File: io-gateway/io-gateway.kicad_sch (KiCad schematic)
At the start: 8 parts, among them J1 1752201, J2 1752201, J3 1752201, J4 Screw_Terminal_01x09, J5 Screw_Terminal_01x09, J6 Screw_Terminal_01x09

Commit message: upd
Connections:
- net GND_DIM5 renamed Dimmer5/GND_DIM
- net VIN_DIM5 renamed Dimmer5/VIN_DIM
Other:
- added sheet Dimmer5 (dimmer1.kicad_sch)
- moved on the sheet: J3

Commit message: upd
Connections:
- net GND: now also J4.3 (Pin_3), J4.6 (Pin_6), J4.9 (Pin_9), J5.3 (Pin_3), J5.6 (Pin_6), J5.9 (Pin_9), J6.3 (Pin_3), J6.6 (Pin_6), J6.9 (Pin_9)
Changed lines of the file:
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@@
+		)
+	)
+	(label "GND_CTRL"
+		(at 220.98 31.75 0)
+		(effects
+			(font
+				(size 1.27 1.27)
+			)
+			(justify left bottom)
 		)
 	)
 	(label "VDC_CTRL"
 		(at 40.64 27.94 0)
+		(effects
+			(font
+				(size 1.27 1.27)
+			)
+			(justify left bottom)
+		)
+	)
+	(label "GND_CTRL"
+		(at 220.98 96.52 0)
 		(effects
 			(font
@@
 		)
 	)
+	(label "GND_CTRL"
+		(at 220.98 39.37 0)
+		(effects
+			(font
+				(size 1.27 1.27)
+			)
+			(justify left bottom)
+		)
+	)
+	(label "GND_CTRL"
+		(at 220.98 129.54 0)
+		(effects
+			(font
+				(size 1.27 1.27)
+			)
+			(justify left bottom)
+		)
+	)
 	(label "ANALOG_IN_1"
 		(at 40.64 38.1 0)
@@
 		)
 	)
+	(label "GND_CTRL"
+		(at 220.98 81.28 0)
+		(effects
+			(font
+				(size 1.27 1.27)
+			)
+			(justify left bottom)
+		)
+	)
+	(label "GND_CTRL"
+		(at 220.98 88.9 0)
+		(effects
+			(font
+				(size 1.27 1.27)
+			)
+			(justify left bottom)
+		)
+	)
+	(label "GND_CTRL"
+		(at 220.98 137.16 0)
+		(effects
+			(font
+				(size 1.27 1.27)
+			)
+			(justify left bottom)
+		)
+	)
+	(label "GND_CTRL"
+		(at 220.98 121.92 0)
+		(effects
+			(font
+				(size 1.27 1.27)
+			)
+			(justify left bottom)
+		)
+	)
 	(label "RS485_B"
 		(at 40.64 35.56 0)
 		(effects
 			(font
+				(size 1.27 1.27)
+			)
+			(justify left bottom)
+		)
+	)
+	(label "GND_CTRL"
+		(at 220.98 46.99 0)
+		(effects
+			(font

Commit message: upd
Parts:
- removed J4, J5, J6: Screw_Terminal_01x09, TerminalBlock_TE-Connectivity:TerminalBlock_TE_282836-9_1x09_P5mm_Horizontal, symbol Connector:Screw_Terminal_01x09
- added J10, J11, J12, J13, J4, J5, J7, J8, J9: Screw_Terminal_01x02, TerminalBlock:TerminalBlock_MaiXu_MX126-5.0-02P_1x02_P5.00mm, symbol Connector:Screw_Terminal_01x02
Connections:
- net Relay4/VAC_IN: now also J4.2 (Pin_2)
- net Relay4/VAC_OUT: now also J4.1 (Pin_1)
- net Relay5/VAC_IN: now also J10.2 (Pin_2)
- net Relay5/VAC_OUT: now also J10.1 (Pin_1)
- net Relay6/VAC_IN: now also J11.2 (Pin_2)
- net Relay6/VAC_OUT: now also J11.1 (Pin_1)
- net Relay7/VAC_IN: now also J5.2 (Pin_2)
- net Relay7/VAC_OUT: now also J5.1 (Pin_1)
- net Relay8/VAC_IN: now also J12.2 (Pin_2)
- net Relay8/VAC_OUT: now also J12.1 (Pin_1)
- net Relay9/VAC_IN: now also J13.2 (Pin_2)
- net Relay9/VAC_OUT: now also J13.1 (Pin_1)
- net VAC_IN_1: now also J7.2 (Pin_2)
- net VAC_IN_2: now also J8.2 (Pin_2)
- net VAC_IN_3: now also J9.2 (Pin_2)
- net VAC_OUT_1.1: now also J7.1 (Pin_1)
- net VAC_OUT_2.1: now also J8.1 (Pin_1)
- net VAC_OUT_3.1: now also J9.1 (Pin_1)

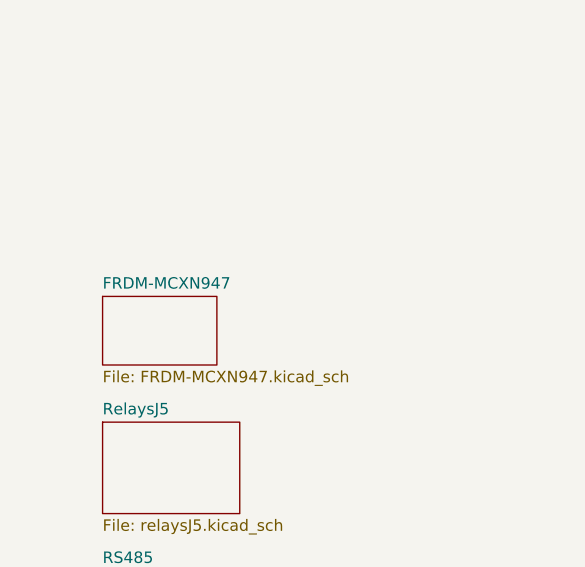
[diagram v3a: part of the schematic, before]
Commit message: connect Relays in Schematics
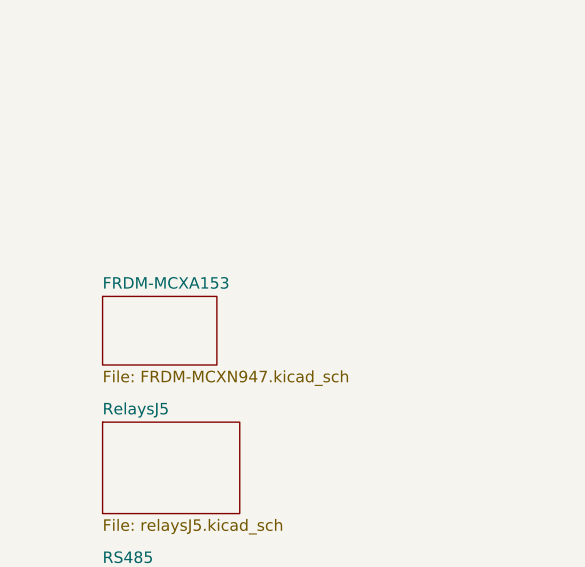
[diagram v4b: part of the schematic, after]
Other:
- sheet FRDM-MCXN947 renamed FRDM-MCXA153
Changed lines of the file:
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@@
 			(color 0 0 0 0.0000)
 		)
-		(property "Sheetname" "FRDM-MCXN947"
+		(property "Sheetname" "FRDM-MCXA153"
 			(at 30.48 218.9984 0)
 			(effects

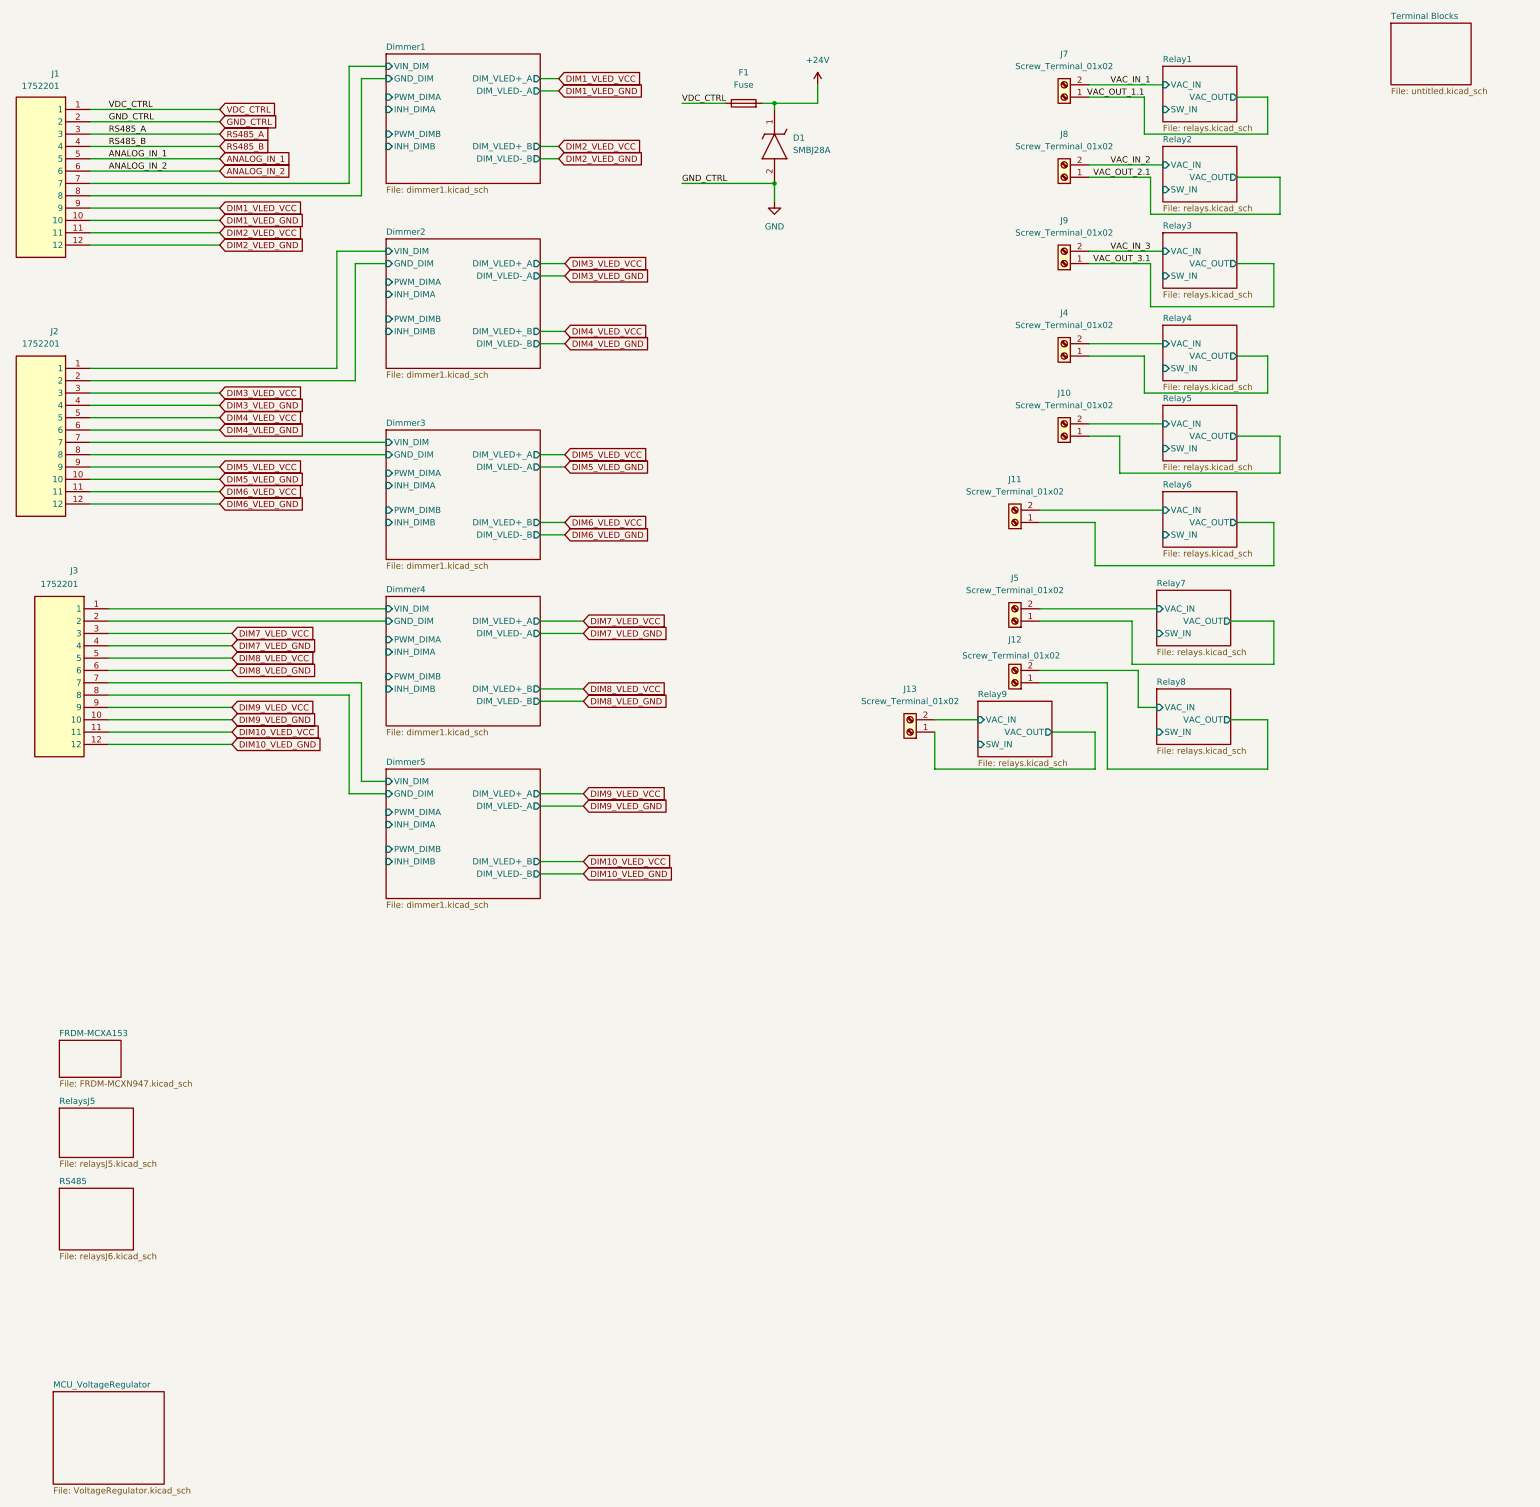
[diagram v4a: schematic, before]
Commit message: add RS485
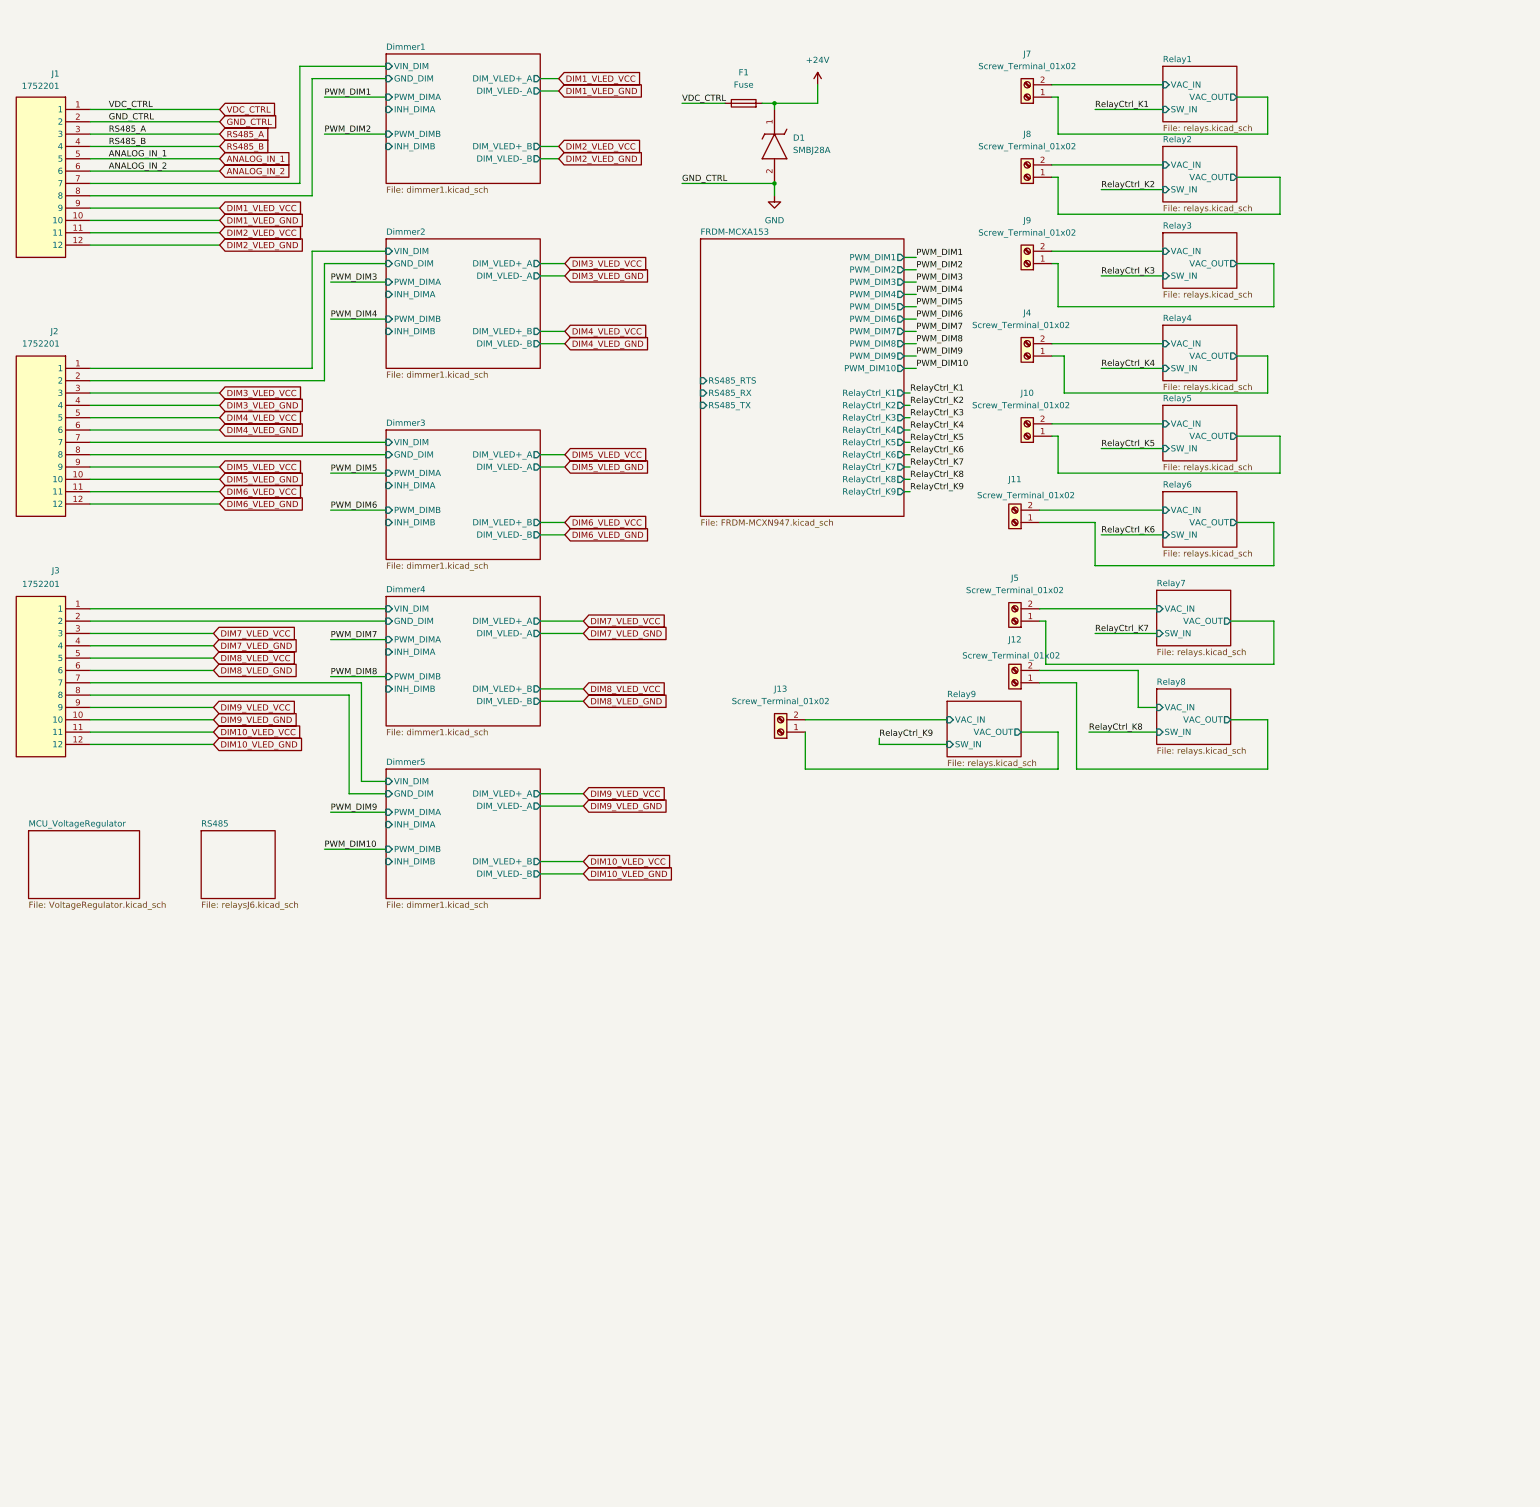
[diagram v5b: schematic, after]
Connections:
- net VAC_IN_1 renamed Relay1/VAC_IN
- net VAC_IN_2 renamed Relay2/VAC_IN
- net VAC_IN_3 renamed Relay3/VAC_IN
- net VAC_OUT_1.1 renamed Relay1/VAC_OUT
- net VAC_OUT_2.1 renamed Relay2/VAC_OUT
- net VAC_OUT_3.1 renamed Relay3/VAC_OUT
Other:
- removed sheet RelaysJ5
- removed sheet Terminal Blocks
- sheet FRDM-MCXA153 ports: added PWM_DIM1, PWM_DIM10, PWM_DIM2, PWM_DIM3, PWM_DIM4, PWM_DIM5, PWM_DIM6, PWM_DIM7, PWM_DIM8, PWM_DIM9, RS485_RTS, RS485_RX, RS485_TX, RelayCtrl_K1, RelayCtrl_K2, RelayCtrl_K3, RelayCtrl_K4, RelayCtrl_K5, RelayCtrl_K6, RelayCtrl_K7, RelayCtrl_K8, RelayCtrl_K9; removed none
- moved on the sheet: J10, J13, J3, J4, J7, J8, J9

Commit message: upd rs485
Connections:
- net RS485_A: now also J1.4; no longer J1.3
- net RS485_B: now also J1.3; no longer J1.4
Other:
- sheet RS485 ports: added RS485_A, RS485_B, RS485_RTS, RS485_RxD, RS485__TXD; removed none
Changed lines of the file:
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@@
 	(wire
 		(pts
+			(xy 162.56 128.27) (xy 158.75 128.27)
+		)
+		(stroke
+			(width 0)
+			(type default)
+		)
+	)
+	(wire
+		(pts
 			(xy 204.47 58.42) (xy 207.01 58.42)
 		)
@@
 	(wire
 		(pts
-			(xy 36.83 33.02) (xy 63.5 33.02)
+			(xy 279.4 86.36) (xy 237.49 86.36)
 		)
 		(stroke
@@
 	(wire
 		(pts
-			(xy 279.4 86.36) (xy 237.49 86.36)
+			(xy 273.05 25.4) (xy 279.4 25.4)
 		)
 		(stroke
@@
 	(wire
 		(pts
-			(xy 273.05 25.4) (xy 279.4 25.4)
+			(xy 160.02 123.19) (xy 160.02 91.44)
+		)
+		(stroke
+			(width 0)
+			(type default)
+		)
+	)
+	(wire
+		(pts
+			(xy 204.47 128.27) (xy 207.01 128.27)
+		)
+		(stroke
+			(width 0)
+			(type default)
+		)
+	)
+	(wire
+		(pts
+			(xy 158.75 87.63) (xy 162.56 87.63)
 		)
 		(stroke
@@
 	(wire
 		(pts
+			(xy 36.83 33.02) (xy 40.64 33.02)
+		)
+		(stroke
+			(width 0)
+			(type default)
+		)
+	)
+	(wire
+		(pts
 			(xy 85.09 180.34) (xy 97.79 180.34)
 		)
@@
 	(wire
 		(pts
+			(xy 162.56 123.19) (xy 160.02 123.19)
+		)
+		(stroke
+			(width 0)
+			(type default)
+		)
+	)
+	(wire
+		(pts
 			(xy 234.95 78.74) (xy 237.49 78.74)
 		)
@@
 	(wire
 		(pts
+			(xy 157.48 130.81) (xy 157.48 83.82)
+		)
+		(stroke
+			(width 0)
+			(type default)
+		)
+	)
+	(wire
+		(pts
 			(xy 36.83 93.98) (xy 63.5 93.98)
 		)
@@
 	(wire
 		(pts
+			(xy 36.83 35.56) (xy 40.64 35.56)
+		)
+		(stroke
+			(width 0)
+			(type default)
+		)
+	)
+	(wire
+		(pts
 			(xy 36.83 86.36) (xy 63.5 86.36)
 		)
@@
 	(wire
 		(pts
-			(xy 36.83 35.56) (xy 63.5 35.56)
+			(xy 280.67 59.69) (xy 280.67 68.58)
 		)
 		(stroke
@@
 	(wire
 		(pts
-			(xy 280.67 59.69) (xy 280.67 68.58)
+			(xy 158.75 128.27) (xy 158.75 87.63)
+		)
+		(stroke
+			(width 0)
+			(type default)
+		)
+	)
+	(wire
+		(pts
+			(xy 160.02 91.44) (xy 162.56 91.44)
 		)
 		(stroke
@@
 	(wire
 		(pts
+			(xy 204.47 125.73) (xy 207.01 125.73)
+		)
+		(stroke
+			(width 0)
+			(type default)
+		)
+	)
+	(wire
+		(pts
 			(xy 240.03 146.05) (xy 232.41 146.05)
 		)
@@
 	(wire
 		(pts
+			(xy 157.48 83.82) (xy 162.56 83.82)
+		)
+		(stroke
+			(width 0)
+			(type default)
+		)
+	)
+	(wire
+		(pts
 			(xy 232.41 113.03) (xy 243.84 113.03)
 		)
@@
 		)
 	)
+	(wire
+		(pts
+			(xy 162.56 130.81) (xy 157.48 130.81)
+		)
+		(stroke
+			(width 0)
+			(type default)
+		)
+	)
 	(label "GND_CTRL"
 		(at 158.75 43.18 0)
@@
 		)
 	)
+	(label "RS485_B"
+		(at 207.01 128.27 0)
+		(effects
+			(font
+				(size 1.27 1.27)
+			)
+			(justify left bottom)
+		)
+	)
 	(label "PWM_DIM6"
 		(at 207.01 71.12 0)
@@
 	)
 	(label "RS485_A"
-		(at 40.64 33.02 0)
+		(at 40.64 35.56 0)
 		(effects
 			(font
@@
 		)
 	)
+	(label "RS485_A"
+		(at 207.01 125.73 0)
+		(effects
+			(font
+				(size 1.27 1.27)
+			)
+			(justify left bottom)
+		)
+	)
 	(label "PWM_DIM5"
 		(at 86.36 102.87 0)
@@
 	)
 	(label "RS485_B"
-		(at 40.64 35.56 0)
+		(at 40.64 33.02 0)
 		(effects
 			(font
@@
 		)
 	)
-	(global_label "RS485_A"
-		(shape input)
-		(at 63.5 33.02 0)
-		(fields_autoplaced yes)
-		(effects
-			(font
-				(size 1.27 1.27)
-			)
-			(justify left)
-		)
-		(property "Intersheetrefs" "${INTERSHEET_REFS}"
-			(at 74.6494 33.02 0)
-			(effects
-				(font
-					(size 1.27 1.27)
-				)
-				(justify left)
-				(hide yes)
-			)
-		)
-	)
 	(global_label "DIM5_VLED_GND"
 		(shape input)
@@
 		)
 	)
-	(global_label "RS485_B"
-		(shape input)
-		(at 63.5 35.56 0)
-		(fields_autoplaced yes)
-		(effects
-			(font
-				(size 1.27 1.27)
-			)
-			(justify left)
-		)
-		(property "Intersheetrefs" "${INTERSHEET_REFS}"
-			(at 74.8308 35.56 0)
-			(effects
-				(font
-					(size 1.27 1.27)
-				)
-				(justify left)
-				(hide yes)
-			)
-		)
-	)
 	(global_label "DIM1_VLED_GND"
 		(shape input)
@@
 	)
 	(sheet
-		(at 59.69 176.53)
-		(size 15.24 13.97)
+		(at 162.56 119.38)
+		(size 41.91 13.97)
 		(exclude_from_sim no)
 		(in_bom yes)
@@
 		)
 		(property "Sheetname" "RS485"
-			(at 59.69 175.8184 0)
+			(at 162.56 118.6684 0)
 			(effects
 				(font
@@
 		)
 		(property "Sheetfile" "relaysJ6.kicad_sch"
-			(at 59.69 191.0846 0)
+			(at 162.56 133.9346 0)
 			(effects
 				(font
@@
 			)
 		)
+		(pin "RS485_A" bidirectional
+			(at 204.47 125.73 0)
+			(effects
+				(font
+					(size 1.27 1.27)
+				)
+				(justify right)
+			)
+		)
+		(pin "RS485_B" bidirectional
+			(at 204.47 128.27 0)
+			(effects
+				(font
+					(size 1.27 1.27)
+				)
+				(justify right)
+			)
+		)
+		(pin "RS485_RxD" input
+			(at 162.56 128.27 180)
+			(effects
+				(font
+					(size 1.27 1.27)
+				)
+				(justify left)
+			)
+		)
+		(pin "RS485__TXD" input
+			(at 162.56 130.81 180)
+			(effects
+				(font
+					(size 1.27 1.27)
+				)
+				(justify left)
+			)
+		)
+		(pin "RS485_RTS" input
+			(at 162.56 123.19 180)
+			(effects
+				(font
+					(size 1.27 1.27)
+				)
+				(justify left)
+			)
+		)
 		(instances
 			(project "io-gateway"
@@
 	)
 	(sheet
-		(at 24.13 176.53)
+		(at 20.32 165.1)
 		(size 22.86 13.97)
 		(exclude_from_sim no)
@@
 		)
 		(property "Sheetname" "MCU_VoltageRegulator"
-			(at 24.13 175.8184 0)
+			(at 20.32 164.3884 0)
 			(effects
 				(font
@@
 		)
 		(property "Sheetfile" "VoltageRegulator.kicad_sch"
-			(at 24.13 191.0846 0)
+			(at 20.32 179.6546 0)
 			(effects
 				(font
@@
 		)
 		(pin "RS485_RTS" input
-			(at 162.56 83.82 180)
+			(at 162.56 91.44 180)
 			(effects
 				(font
@@
 		)
 		(pin "RS485_RX" input
-			(at 162.56 86.36 180)
+			(at 162.56 87.63 180)
 			(effects
 				(font
@@
 		)
 		(pin "RS485_TX" input
-			(at 162.56 88.9 180)
+			(at 162.56 83.82 180)
 			(effects
 				(font
